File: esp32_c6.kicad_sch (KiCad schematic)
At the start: 39 parts, among them J21 USB_B_Mini, J6 FT232RL, Q4 Q_NPN_BCE, Q5 Q_NPN_BCE, SW1 SW_Push, SW11 boot, U1 ESP32-C6-WROOM-1-N8, U2 ESP32-C6-DEVKITC-1-N8, U9 LM1117DT-3.3, Y2 Crystal

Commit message: Update KiCad schematics/PCB and project files
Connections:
- net +3.3V is gone; now on net +3V3: R20.1
- net IO_12 renamed uD-
- net IO_13 renamed uD+
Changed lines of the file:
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@@
 	(wire
 		(pts
-			(xy 50.8 55.88) (xy 55.88 55.88)
+			(xy 41.91 55.88) (xy 55.88 55.88)
 		)
 		(stroke
@@
 	(wire
 		(pts
+			(xy 342.9 143.51) (xy 364.49 143.51)
+		)
+		(stroke
+			(width 0)
+			(type default)
+		)
+	)
+	(wire
+		(pts
 			(xy 91.44 161.29) (xy 105.41 161.29)
 		)
@@
 	(wire
 		(pts
+			(xy 342.9 140.97) (xy 364.49 140.97)
+		)
+		(stroke
+			(width 0)
+			(type default)
+		)
+	)
+	(wire
+		(pts
 			(xy 191.77 125.73) (xy 189.23 125.73)
 		)
@@
 	(wire
 		(pts
-			(xy 50.8 53.34) (xy 55.88 53.34)
+			(xy 41.91 53.34) (xy 55.88 53.34)
 		)
 		(stroke
@@
 	)
 	(label "IO_12"
-		(at 342.9 143.51 0)
+		(at 347.98 143.51 0)
 		(effects
 			(font
@@
 		)
 	)
+	(label "d-"
+		(at 47.625 55.88 0)
+		(effects
+			(font
+				(size 1.27 1.27)
+			)
+			(justify left bottom)
+		)
+	)
 	(label "IO_11"
 		(at 191.77 110.49 0)
@@
 	)
 	(label "IO_13"
-		(at 342.9 140.97 0)
+		(at 347.98 140.97 0)
 		(effects
 			(font
@@
 		)
 	)
+	(label "d+"
+		(at 45.72 53.34 0)
+		(effects
+			(font
+				(size 1.27 1.27)
+			)
+			(justify left bottom)
+		)
+	)
 	(label "IO_17"
 		(at 243.84 137.16 180)
@@
 	)
 	(label "IO_12"
-		(at 50.8 55.88 180)
+		(at 41.91 55.88 180)
 		(effects
 			(font
@@
 	)
 	(label "IO_13"
-		(at 50.8 53.34 180)
+		(at 41.91 53.34 180)
 		(effects
 			(font
@@
 		)
 	)
+	(global_label "uD-"
+		(shape input)
+		(at 364.49 143.51 0)
+		(fields_autoplaced yes)
+		(effects
+			(font
+				(size 1.27 1.27)
+			)
+			(justify left)
+		)
+		(property "Intersheetrefs" "${INTERSHEET_REFS}"
+			(at 371.4666 143.51 0)
+			(hide yes)
+			(show_name no)
+			(do_not_autoplace no)
+			(effects
+				(font
+					(size 1.27 1.27)
+				)
+				(justify left)
+			)
+		)
+	)
+	(global_label "uD+"
+		(shape input)
+		(at 364.49 140.97 0)
+		(fields_autoplaced yes)
+		(effects
+			(font
+				(size 1.27 1.27)
+			)
+			(justify left)
+		)
+		(property "Intersheetrefs" "${INTERSHEET_REFS}"
+			(at 371.4666 140.97 0)
+			(hide yes)
+			(show_name no)
+			(do_not_autoplace no)
+			(effects
+				(font
+					(size 1.27 1.27)
+				)
+				(justify left)
+			)
+		)
+	)
 	(hierarchical_label "IO_5"
 		(shape input)
@@
 		(property "Footprint" "kiC:XCVR_ESP32-C6-WROOM-1-N8"
 			(at 168.91 123.19 0)
-			(hide yes)
 			(show_name no)
 			(do_not_autoplace no)
@@
 	)
 	(symbol
-		(lib_id "power:+3.3V")
-		(at 354.33 198.12 0)
-		(unit 1)
-		(body_style 1)
-		(exclude_from_sim no)
-		(in_bom yes)
-		(on_board yes)
-		(in_pos_files yes)
-		(dnp no)
-		(property "Reference" "#PWR029"
-			(at 354.33 201.93 0)
-			(hide yes)
-			(show_name no)
-			(do_not_autoplace no)
-			(effects
-				(font
-					(size 1.27 1.27)
-				)
-			)
-		)
-		(property "Value" "+3.3V"
-			(at 355.6 194.31 0)
-			(show_name no)
-			(do_not_autoplace no)
-			(effects
-				(font
-					(size 1.27 1.27)
-				)
-			)
-		)
-		(property "Footprint" ""
-			(at 354.33 198.12 0)
-			(hide yes)
-			(show_name no)
-			(do_not_autoplace no)
-			(effects
-				(font
-					(size 1.27 1.27)
-				)
-			)
-		)
-		(property "Datasheet" ""
-			(at 354.33 198.12 0)
-			(hide yes)
-			(show_name no)
-			(do_not_autoplace no)
-			(effects
-				(font
-					(size 1.27 1.27)
-				)
-			)
-		)
-		(property "Description" ""
-			(at 354.33 198.12 0)
-			(show_name no)
-			(do_not_autoplace no)
-			(effects
-				(font
-					(size 1.27 1.27)
-				)
-			)
-		)
-		(pin "1"
-		)
-		(instances
-			(project "esp32_xiaozhi"
-				(path "/cae338e8-f342-43cb-b99a-a0486629133c/99dbbdf2-0f67-4248-a995-74d5ebf0be3f"
-					(reference "#PWR029")
-					(unit 1)
-				)
-			)
-		)
-	)
-	(symbol
 		(lib_id "power:GND")
 		(at 123.19 71.755 0)
@@
 					(unit 1)
 				)
+			)
+		)
+	)
+	(symbol
+		(lib_id "power:+3V3")
+		(at 354.33 198.12 0)
+		(unit 1)
+		(body_style 1)
+		(exclude_from_sim no)
+		(in_bom yes)
+		(on_board yes)
+		(in_pos_files yes)
+		(dnp no)
+		(fields_autoplaced yes)
+		(property "Reference" "#PWR025"
+			(at 354.33 201.93 0)
+			(hide yes)
+			(show_name no)
+			(do_not_autoplace no)
+			(effects
+				(font
+					(size 1.27 1.27)
+				)
+			)
+		)
+		(property "Value" "+3V3"
+			(at 354.33 193.04 0)
+			(show_name no)
+			(do_not_autoplace no)
+			(effects
+				(font
+					(size 1.27 1.27)
+				)
+			)
+		)
+		(property "Footprint" ""
+			(at 354.33 198.12 0)
+			(hide yes)
+			(show_name no)
+			(do_not_autoplace no)
+			(effects
+				(font
+					(size 1.27 1.27)
+				)
+			)
+		)
+		(property "Datasheet" ""
+			(at 354.33 198.12 0)
+			(hide yes)
+			(show_name no)
+			(do_not_autoplace no)
+			(effects
+				(font
+					(size 1.27 1.27)
+				)
+			)
+		)
+		(property "Description" "Power symbol creates a global label with name \"+3V3\""
+			(at 354.33 198.12 0)
+			(hide yes)
+			(show_name no)
+			(do_not_autoplace no)
+			(effects
+				(font
+					(size 1.27 1.27)
+				)
+			)
+		)
+		(pin "1"
+		)
+		(instances
+			(project "esp32_xiaozhi"
+				(path "/cae338e8-f342-43cb-b99a-a0486629133c/99dbbdf2-0f67-4248-a995-74d5ebf0be3f"
+					(reference "#PWR025")
+					(unit 1)
+				)

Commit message: add files update
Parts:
- C45: value 100nf -> 1uf
- C50, C51: value 100n -> 15pf
- J21, R26, R37, U2, Y2: now left out of the parts list
- R15, R16: value 10k -> 2k2
- R62, R63: value 5.1k -> 27
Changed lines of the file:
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@@
 		(body_style 1)
 		(exclude_from_sim no)
-		(in_bom yes)
+		(in_bom no)
 		(on_board yes)
-		(in_pos_files yes)
+		(in_pos_files no)
 		(dnp no)
 		(fields_autoplaced yes)
@@
 			)
 		)
-		(property "Value" "100n"
+		(property "Value" "15pf"
 			(at 163.195 198.755 0)
 			(show_name no)
@@
 		(body_style 1)
 		(exclude_from_sim no)
-		(in_bom yes)
+		(in_bom no)
 		(on_board yes)
-		(in_pos_files yes)
+		(in_pos_files no)
 		(dnp no)
 		(fields_autoplaced yes)
@@
 			)
 		)
-		(property "Value" "5.1k"
+		(property "Value" "27"
 			(at 59.69 51.435 90)
 			(show_name no)
@@
 			)
 		)
-		(property "Value" "5.1k"
+		(property "Value" "27"
 			(at 59.182 59.182 90)
 			(show_name no)
@@
 			)
 		)
-		(property "Value" "10k"
+		(property "Value" "2k2"
 			(at 311.785 210.82 90)
 			(show_name no)
@@
 			)
 		)
-		(property "Value" "100n"
+		(property "Value" "15pf"
 			(at 198.755 198.755 0)
 			(show_name no)
@@
 		(body_style 1)
 		(exclude_from_sim no)
-		(in_bom yes)
+		(in_bom no)
 		(on_board yes)
-		(in_pos_files yes)
+		(in_pos_files no)
 		(dnp no)
 		(property "Reference" "R37"
@@
 			)
 		)
-		(property "Value" "100nf"
+		(property "Value" "1uf"
 			(at 197.358 51.308 0)
 			(show_name no)
@@
 		(body_style 1)
 		(exclude_from_sim no)
-		(in_bom yes)
+		(in_bom no)
 		(on_board yes)
-		(in_pos_files yes)
+		(in_pos_files no)
 		(dnp no)
 		(fields_autoplaced yes)
@@
 			)
 		)
-		(property "Description" "Two pin crystal"
+		(property "Description" "Two pin crystal 6MHZ"
 			(at 175.26 194.31 0)
 			(hide yes)
@@
 		(body_style 1)
 		(exclude_from_sim no)
-		(in_bom yes)
+		(in_bom no)
 		(on_board yes)
-		(in_pos_files yes)
+		(in_pos_files no)
 		(dnp no)
 		(property "Reference" "R26"
@@
 			)
 		)
-		(property "Value" "10k"
+		(property "Value" "2k2"
 			(at 309.88 223.52 90)
 			(show_name no)

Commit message: Actualización de esquemas y PCB con datos LCSC y librerías JLC
- Añade propiedades LCSC a los símbolos de las hojas de esquema
- Actualiza las hojas TXS0108E, display, esp32_c6, ft232, inmp441,
  led_sw_gpio, max98357a, micro_sd, power_supply y el esquema raíz
- Reorganiza el PCB (footprints, jumpers y nets) y actualiza el proyecto
- Incluye las librerías locales JLCImport (símbolos, huellas y modelos 3D)
  y las entradas correspondientes en fp-lib-table y sym-lib-table
- Añade la documentación técnica en docs/ y el archivo de posiciones
  esp32_xiaozhi-all.pos
- Elimina los ZIP generados gebers.zip y production.zip
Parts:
- added JP19, JP20: jp_xt, Jumper:SolderJumper-2_P1.3mm_Open_RoundedPad1.0x1.5mm, symbol Jumper:Jumper_2_Open
- added JP21: jp_xt, Jumper:SolderJumper-2_P1.3mm_Bridged2Bar_RoundedPad1.0x1.5mm, symbol Jumper:Jumper_2_Open
- added R70: 5.1k, Resistor_SMD:R_0805_2012Metric, symbol Device:R
- C1, C2, C3, C46, C49: LCSC (none) -> C1525
- C45: LCSC (none) -> C1848
- D10, D11, D9: LCSC (none) -> C41399463; Manufacturer LRC(乐山无线电) -> (none)
- D12: footprint Diode_SMD:D_SOD-923 -> Diode_SMD:D_SOD-523; LCSC (none) -> C19829537
- D14: footprint Diode_SMD:D_2512_6332Metric -> Diode_SMD:D_1206_3216Metric; LCSC (none) -> C143806
- D8: LCSC (none) -> C81598
- J21: LCSC (none) -> C91144; now not fitted
- J6: now left out of the parts list
- L7: LCSC (none) -> C74489
- R15, R16: LCSC C25744 -> C4190
- R20: LCSC C25744 -> C17414
- R26, R37: LCSC (none) -> C2933393; now not fitted
- R58, R59: LCSC (none) -> C27834
- R62, R63: LCSC (none) -> C2933393
- R64: LCSC (none) -> C17414
- SW11: LCSC (none) -> C720477
- U1: LCSC (none) -> C5366877
- U2: LCSC (none) -> C20554022
- U9: LCSC (none) -> C969102
- USBC1: footprint kiC:USB-C-SMD_TYPE-C-USB-17 -> JLCImport:USB-C-SMD_TYPE-C-USB-17_claude2; JLC Part Extended Part -> (none); LCSC (none) -> C167321; LCSC Part # C167321 -> (none); Manufacturer 精拓金 -> (none)
- Y2: value Crystal -> Oscilador 32768hz; footprint Crystal:Crystal_SMD_EuroQuartz_EQ161-2Pin_3.2x1.5mm -> Crystal:Crystal_SMD_3215-2Pin_3.2x1.5mm; LCSC (none) -> C32346; now in the parts list
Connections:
- net GND: now also JP21.1 (A), R70.2; no longer J21.5 (GND1), USBC1.0
- net IO_0: now also JP19.2 (B); no longer C50.1, U1.8 (IO0), U2.J1_7 (GPIO0), Y2.1
- net IO_1: now also JP20.2 (B); no longer C51.1, U1.9 (IO1), U2.J1_8 (GPIO1), Y2.2
- new net: J21.5 (GND1), JP21.2 (B)
- new net IO_0_osc: C50.1, JP19.1 (A), U1.8 (IO0), U2.J1_7 (GPIO0), Y2.1
- new net IO_1_osc: C51.1, JP20.1 (A), U1.9 (IO1), U2.J1_8 (GPIO1), Y2.2
- new net shield_usb_c: R70.1, USBC1.0
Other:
- moved on the sheet: C45, C46, C49, D10, D11, D14, D9, L7, R58, R59, R62, R63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

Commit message: Actualización de esquemas, PCB y librerías
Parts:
- C1, C10, C13, C14, C2, C3, C46, C49: LCSC C1525 -> C28233
- C50, C51: LCSC C1525 -> C107110
- Q5: value Q_NPN_BCE -> Q_PNP_BCE; LCSC C916392 -> C8326
- R15, R16: LCSC C4190 -> C17520
- SW1, SW11: LCSC C720477 -> C92584
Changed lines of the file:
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@@
 			)
 		)
-		(property "LCSC" "C1525"
+		(property "LCSC" "C28233"
 			(at 91.44 165.1 0)
 			(hide yes)
@@
 			)
 		)
-		(property "LCSC" "C720477"
+		(property "LCSC" "C92584"
 			(at 85.09 208.28 0)
 			(hide yes)
@@
 			)
 		)
-		(property "LCSC" "C1525"
+		(property "LCSC" "C28233"
 			(at 354.33 217.17 0)
 			(hide yes)
@@
 		(in_bom no)
 		(on_board yes)
-		(in_pos_files yes)
+		(in_pos_files no)
 		(dnp no)
 		(fields_autoplaced yes)
@@
 			)
 		)
-		(property "LCSC" "C1525"
+		(property "LCSC" "C107110 "
 			(at 158.75 198.12 0)
 			(hide yes)
@@
 			)
 		)
-		(property "LCSC" "C1525"
+		(property "LCSC" "C28233"
 			(at 144.78 214.63 0)
 			(hide yes)
@@
 			)
 		)
-		(property "Value" "Q_NPN_BCE"
+		(property "Value" "Q_PNP_BCE"
 			(at 330.835 219.075 0)
 			(show_name no)
@@
 			)
 		)
-		(property "LCSC" "C916392"
+		(property "LCSC" "C8326"
 			(at 325.12 220.98 0)
 			(hide yes)
@@
 			)
 		)
-		(property "LCSC" "C1525"
+		(property "LCSC" "C28233"
 			(at 119.38 165.1 0)
 			(hide yes)
@@
 			)
 		)
-		(property "LCSC" "C4190"
+		(property "LCSC" "C17520"
 			(at 308.61 208.28 0)
 			(hide yes)
@@
 			)
 		)
-		(property "LCSC" "C1525"
+		(property "LCSC" "C107110 "
 			(at 194.31 198.12 0)
 			(hide yes)
@@
 			)
 		)
-		(property "LCSC" "C1525"
+		(property "LCSC" "C28233"
 			(at 284.48 59.69 0)
 			(hide yes)
@@
 			)
 		)
-		(property "LCSC" "C720477"
+		(property "LCSC" "C92584"
 			(at 125.73 209.55 0)
 			(hide yes)
@@
 			)
 		)
-		(property "LCSC" "C1525"
+		(property "LCSC" "C28233"
 			(at 105.41 165.1 0)
 			(hide yes)
@@
 			)
 		)
-		(property "LCSC" "C1525"
+		(property "LCSC" "C28233"
 			(at 91.44 214.63 0)
 			(hide yes)
@@
 			)
 		)
-		(property "LCSC" "C4190"
+		(property "LCSC" "C17520"
 			(at 308.61 220.98 0)
 			(hide yes)
@@
 			)
 		)
-		(property "LCSC" "C1525"
+		(property "LCSC" "C28233"
 			(at 250.19 58.42 0)
 			(hide yes)

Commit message: actualizacion  de pcb logic , rpi
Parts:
- U1: Package SMD-28 Espressif Systems -> (none)
- U2: Package None -> (none)
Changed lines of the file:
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@@
-			)
-		)
-		(property "Package" "None"
-			(at 322.58 130.81 0)
-			(hide yes)
-			(show_name no)
-			(do_not_autoplace no)
-			(effects
-				(font
-					(size 1.27 1.27)
-				)
-				(justify bottom)
 			)
 		)
@@
 			(hide yes)
 			(show_name no)
-			(do_not_autoplace no)
-			(effects
-				(font
-					(size 1.27 1.27)
-				)
-				(justify bottom)
-			)
-		)
-		(property "Package" "SMD-28 Espressif Systems"
-			(at 168.91 123.19 0)
-			(hide yes)
-			(show_name no)

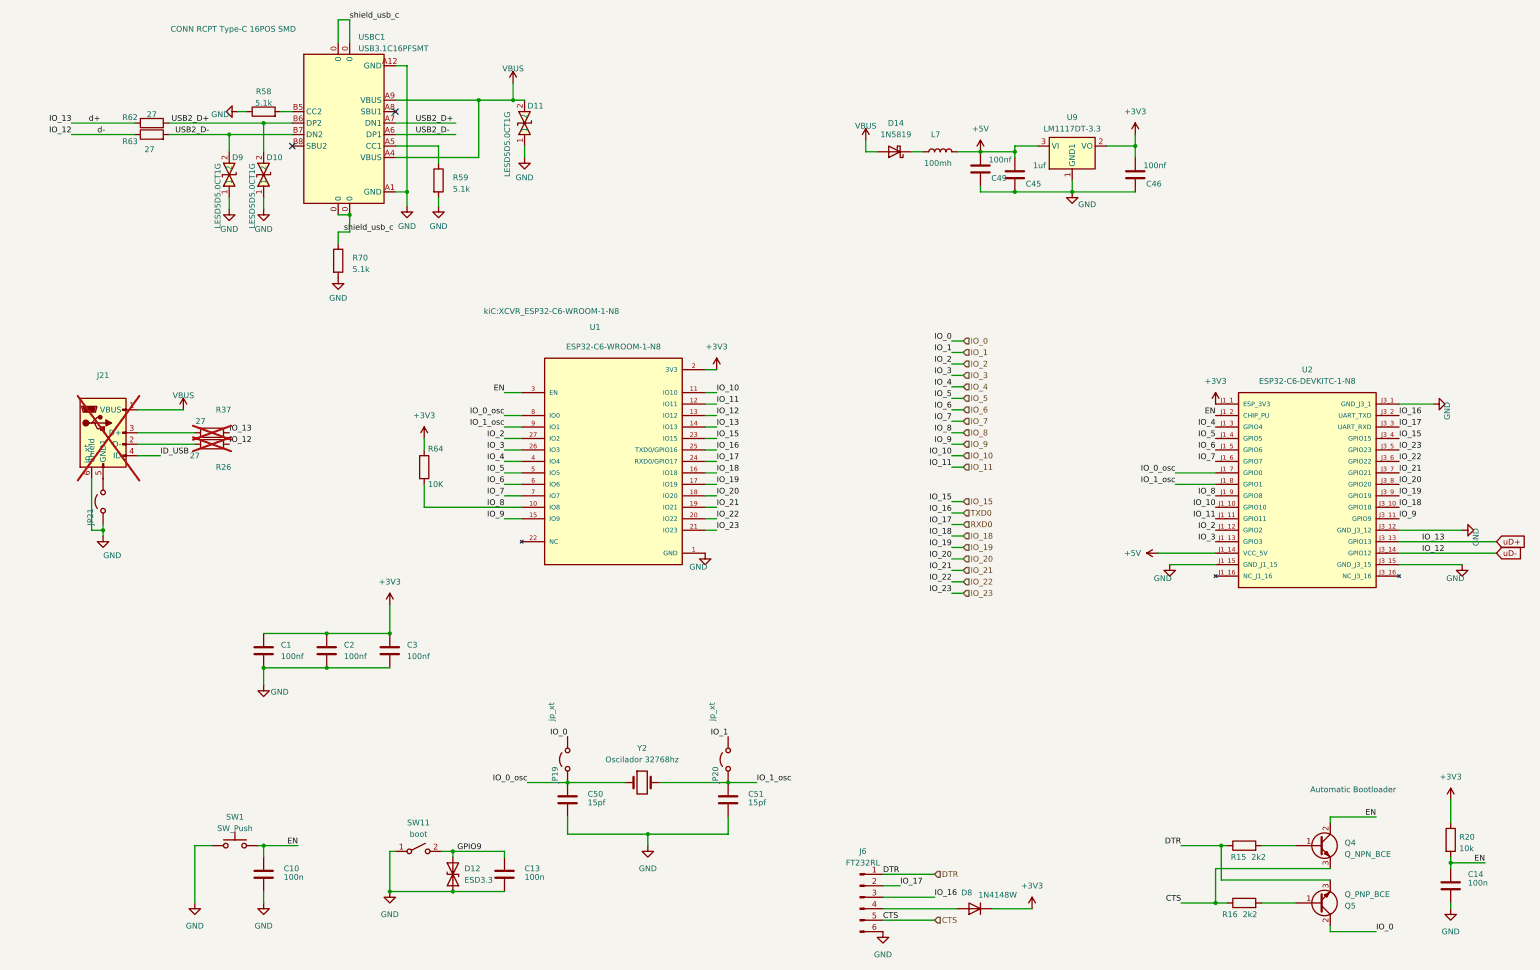
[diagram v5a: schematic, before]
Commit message: correccion de numero de partes de componentes
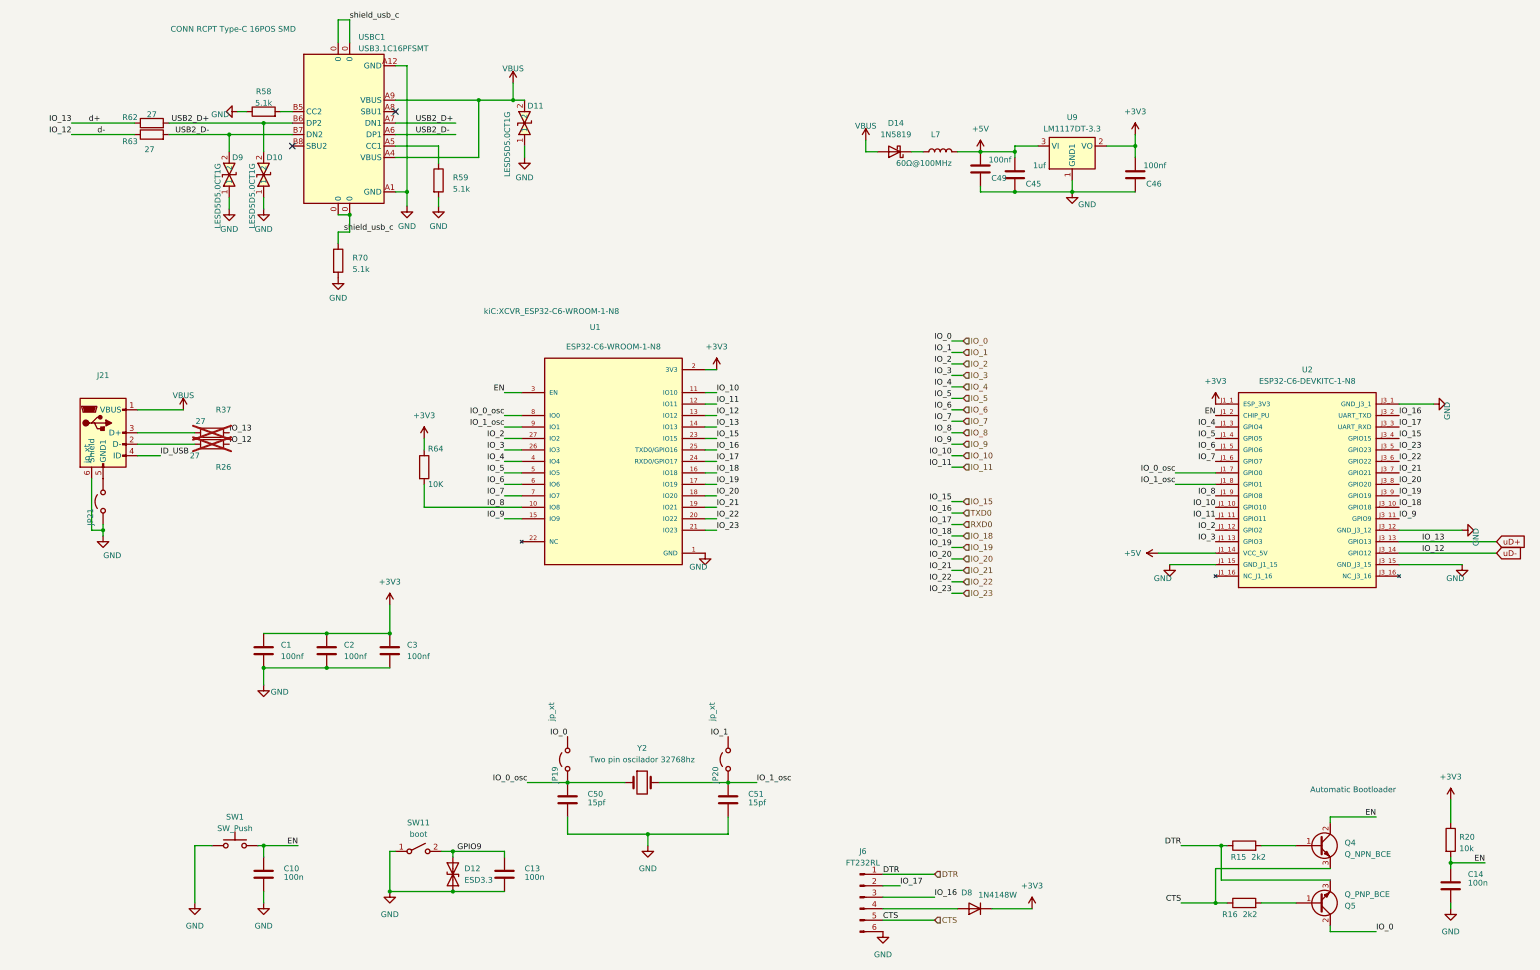
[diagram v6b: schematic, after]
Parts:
- J21: now fitted
- L7: value 100mh -> 60Ω@100MHz
- Y2: value Oscilador 32768hz -> Two pin oscilador 32768hz
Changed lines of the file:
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@@
 		(on_board yes)
 		(in_pos_files no)
-		(dnp yes)
+		(dnp no)
 		(fields_autoplaced yes)
 		(property "Reference" "J21"
@@
 		(in_bom no)
 		(on_board yes)
-		(in_pos_files yes)
+		(in_pos_files no)
 		(dnp no)
 		(property "Reference" "JP20"
@@
 		(in_bom no)
 		(on_board yes)
-		(in_pos_files yes)
+		(in_pos_files no)
 		(dnp no)
 		(property "Reference" "JP19"
@@
 			)
 		)
-		(property "Value" "100mh"
+		(property "Value" "60Ω@100MHz"
 			(at 243.84 57.15 90)
 			(show_name no)
@@
 			)
 		)
-		(property "Description" "1 60Ω@100MHz ±25% 1206 Ferrite Beads ROHS"
+		(property "Description" "60Ω@100MHz"
 			(at 242.316 40.64 90)
 			(hide yes)
@@
 		(in_bom yes)
 		(on_board yes)
-		(in_pos_files no)
+		(in_pos_files yes)
 		(dnp no)
 		(fields_autoplaced yes)
@@
 			)
 		)
-		(property "Value" "Oscilador 32768hz"
+		(property "Value" "Two pin oscilador 32768hz"
 			(at 175.26 189.23 0)
 			(show_name no)

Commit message: add update
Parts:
- J21: now not fitted
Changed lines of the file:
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@@
 		(on_board yes)
 		(in_pos_files no)
-		(dnp no)
+		(dnp yes)
 		(fields_autoplaced yes)
 		(property "Reference" "J21"

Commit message: correccion de partes
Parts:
- J21: value USB_B_Mini -> U-M-M5SS-W-2
- JP21: value jp_xt -> NL
- U9: value LM1117DT-3.3 -> LM1117MDT-3.3/TR; LCSC C969102 -> C498159
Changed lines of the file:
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@@
 			)
 		)
-		(property "Value" "USB_B_Mini"
+		(property "Value" "U-M-M5SS-W-2"
 			(at 55.88 106.68 0)
 			(hide yes)
@@
 			)
 		)
-		(property "Value" "LM1117DT-3.3"
+		(property "Value" "LM1117MDT-3.3/TR"
 			(at 270.51 49.53 0)
 			(show_name no)
@@
 			)
 		)
-		(property "LCSC" "C969102"
+		(property "LCSC" "C498159"
 			(at 270.51 53.34 0)
 			(hide yes)
@@
 		(in_bom no)
 		(on_board yes)
-		(in_pos_files yes)
+		(in_pos_files no)
 		(dnp no)
 		(property "Reference" "JP21"
@@
 			)
 		)
-		(property "Value" "jp_xt"
+		(property "Value" "NL"
 			(at 52.324 119.38 0)
 			(show_name no)
